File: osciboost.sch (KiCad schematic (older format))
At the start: 48 parts, among them P1 Molex 73137-5003, P2 BOOST_LEFT, P3 BOOST_RIGHT, P4 Molex 73137-5003, Q1 DMG1013T, U1 MA1702, U2 MAX6102, U3 LMV821AICT, U4 LMV821AICT, U5 LMV821AICT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

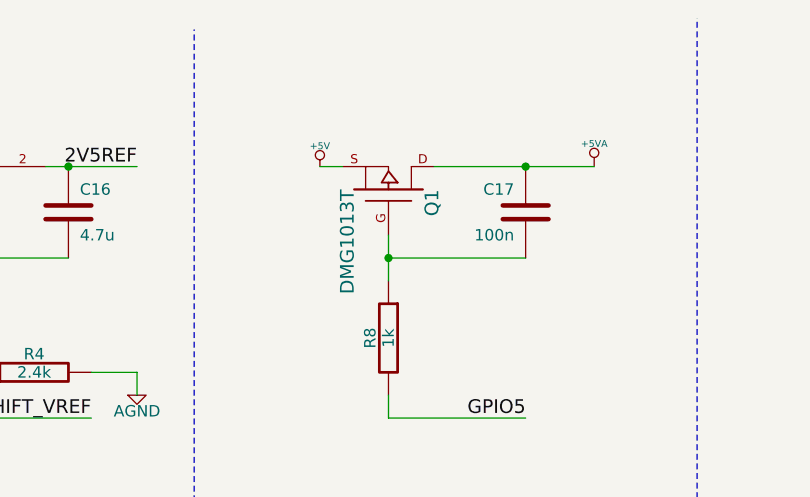
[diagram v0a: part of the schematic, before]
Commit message: Add pull-up resistor for the soft-start circuit
The microcontroller can never bring the voltage on the gate of the soft-start
MOSFET to the 5V needed to turn off power. To only way to achieve 5V is to have
a pull-up resistor, and let the control pin in high-impedance mode.
When the control pin is configured as an output, and (preferrably) set low, the
osciboost module will be powered on. To power off the module, the pin is put
into high-impedance mode.

Add a 10k pull-up resistor to enable the power-off circuit to function
correctly.

Signed-off-by: Alexandru Gagniuc <mr.nuke.me@gmail.com>
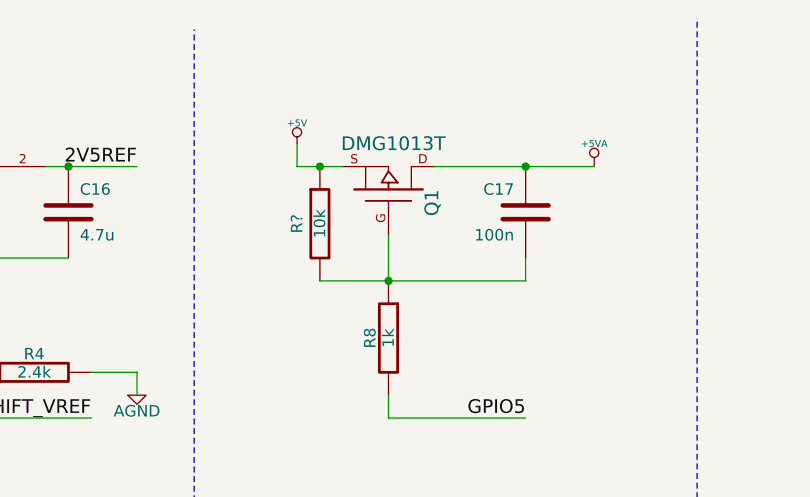
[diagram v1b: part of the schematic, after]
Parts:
- added R?: 10k, symbol R
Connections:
- net +5V: now also R?.1
- net at C17.2, Q1.G, R8.1: now also R?.2
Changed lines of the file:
@@
-EESchema Schematic File Version 2  date Mon 21 Jan 2013 01:50:25 PM CST
+EESchema Schematic File Version 2  date Mon 21 Jan 2013 09:27:00 PM CST
 LIBS:power
 LIBS:device
@@
 encoding utf-8
 Sheet 1 1
-Title "noname.sch"
-Date "21 jan 2013"
-Rev ""
-Comp ""
+Title "osciboost.sch"
+Date "22 jan 2013"
+Rev "NA"
+Comp "G-Tech Hardware Solutions"
 Comment1 ""
 Comment2 ""
@@
 Comment4 ""
 $EndDescr
+Connection ~ 5600 1600
+Wire Wire Line
+	5300 1600 6200 1600
+Wire Wire Line
+	6200 1600 6200 1500
+Connection ~ 5300 1100
 Wire Wire Line
 	9000 1400 8800 1400
@@
 	4750 2900 4750 500
 Wire Wire Line
-	6200 1500 5600 1500
-Connection ~ 5600 1500
-Wire Wire Line
 	6500 1100 5800 1100
 Connection ~ 6200 1100
-Wire Wire Line
-	5300 1100 5400 1100
 Wire Wire Line
 	6200 3750 6400 3750
@@
 Wire Wire Line
 	9000 1300 8800 1300
+Wire Wire Line
+	5200 1000 5200 1100
+Wire Wire Line
+	5200 1100 5400 1100
+$Comp
+L R R?
+U 1 1 50FE06D2
+P 5300 1350
+F 0 "R?" V 5200 1350 50  0000 C CNN
+F 1 "10k" V 5300 1350 50  0000 C CNN
+	1    5300 1350
+	1    0    0    -1
+$EndComp
 Text Label 9000 1400 2    60   ~ 0
 AIN2
@@
 L +5V #PWR024
 U 1 1 50FAE458
-P 5300 1100
-F 0 "#PWR024" H 5300 1190 20  0001 C CNN
-F 1 "+5V" H 5300 1190 30  0000 C CNN
-	1    5300 1100
+P 5200 1000
+F 0 "#PWR024" H 5200 1090 20  0001 C CNN
+F 1 "+5V" H 5200 1090 30  0000 C CNN
+	1    5200 1000
 	-1   0    0    -1
 $EndComp
@@
 P 5600 1200
 F 0 "Q1" H 5600 1390 60  0000 R CNN
-F 1 "DMG1013T" H 5600 1020 60  0000 R CNN
+F 1 "DMG1013T" V 5800 1450 60  0000 R CNN
 	1    5600 1200
 	0    1    -1   0

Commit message: Replace OPAMP with OPA1662 in MSOP-8 package
The previously selected opamps could only handle 6V, not the 10V we are feeding
them. Change the opamps to OPA1662, which have the desired characteristics.
Also, using dual opamps allows us to reduce the number of filter capacitors.

Because the change in footprint, re-laying part of the board was also needed.
The advantage is that the pinout of the MSOP-8 package is identical with many
other opamps.

Signed-off-by: Alexandru Gagniuc <mr.nuke.me@gmail.com>
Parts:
- removed C11, C15, C4, C6: 4.7u, symbol C
- U3: value LMV821AICT -> OPA1662; symbol LMV821AICT -> TL072
- U3: renamed from U4; value LMV821AICT -> OPA1662; symbol LMV821AICT -> TL072
- U4: renamed from U6; value LMV821AICT -> OPA1662; symbol LMV821AICT -> TL072
- U4: renamed from U5; value LMV821AICT -> OPA1662; symbol LMV821AICT -> TL072
- gave numbers to parts that had none: 1
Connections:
- net +5VA: now also U3.8 (V+), U3.8 (V+), U4.8 (V+), U4.8 (V+); no longer U3.5 (V+), U3.5 (V+), U4.5 (V+), U4.5 (V+)
- net -5VA: now also U3.4 (V-), U3.4 (V-), U4.4 (V-), U4.4 (V-); no longer U3.2 (V-), U3.2 (V-), U4.2 (V-), U4.2 (V-)
- net SHIFT_VREF: now also U3.3 (+), U4.3 (+); no longer U3.1 (+), U4.1 (+)
- net at C10.1, C9.2, R1.2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: now also U3.5 (+); no longer U3.1 (+)
- net at R5.2, R6.1: now also U3.6 (-); no longer U3.3 (-)
- net at R5.1, R7.1: now also U3.7; no longer U3.4
- net at R7.2, R9.2: now also U3.2 (-); no longer U3.3 (-)
- net at R10.1, R9.1: now also U3.1; no longer U3.4
- net at R16.1, R17.1: now also U4.1; no longer U4.4
- net at R13.2, R14.1: now also U4.6 (-); no longer U4.3 (-)
- net at R13.1, R15.1: now also U4.7; no longer U4.4
- net at R15.2, R16.2: now also U4.2 (-); no longer U4.3 (-)
- net at C19.2, C20.1, R11.2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: now also U4.5 (+); no longer U4.1 (+)
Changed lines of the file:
@@
-EESchema Schematic File Version 2  date Mon 21 Jan 2013 09:27:00 PM CST
+EESchema Schematic File Version 2  date Sat 26 Jan 2013 03:39:28 PM CST
 LIBS:power
 LIBS:device
@@
 Sheet 1 1
 Title "osciboost.sch"
-Date "22 jan 2013"
+Date "26 jan 2013"
 Rev "NA"
 Comp "G-Tech Hardware Solutions"
@@
 Comment4 ""
 $EndDescr
+Wire Wire Line
+	9300 3700 9000 3700
+Wire Wire Line
+	7300 3300 7600 3300
 Connection ~ 5600 1600
 Wire Wire Line
@@
 Connection ~ 9000 3700
 Connection ~ 9300 3700
-Wire Wire Line
-	9600 3700 8700 3700
 Connection ~ 9300 3300
 Wire Wire Line
-	8700 3300 9600 3300
-Connection ~ 7900 3700
-Wire Wire Line
-	7300 3700 8200 3700
-Connection ~ 7900 3300
-Wire Wire Line
-	7300 3300 8200 3300
-Wire Wire Line
 	9000 3200 9000 3300
 Wire Wire Line
-	7600 3200 7600 3300
+	7600 3300 7600 3200
 Wire Wire Line
 	7600 3800 7600 3700
@@
 Wire Wire Line
 	5200 1100 5400 1100
-$Comp
-L R R?
+Wire Wire Line
+	7600 3700 7300 3700
+Wire Wire Line
+	9000 3300 9300 3300
+$Comp
+L R R18
 U 1 1 50FE06D2
 P 5300 1350
-F 0 "R?" V 5200 1350 50  0000 C CNN
+F 0 "R18" V 5200 1350 50  0000 C CNN
 F 1 "10k" V 5300 1350 50  0000 C CNN
 	1    5300 1350
@@
 $EndComp
 $Comp
-L LMV821AICT U5
-U 1 1 50FD9AB6
+L TL072 U4
+U 2 1 50FD9AB6
 P 3100 6300
-F 0 "U5" H 3050 6500 60  0000 L CNN
-F 1 "LMV821AICT" H 3050 6050 60  0000 L CNN
-	1    3100 6300
-	1    0    0    -1
-$EndComp
-$Comp
-L LMV821AICT U6
+F 0 "U4" H 3050 6500 60  0000 L CNN
+F 1 "OPA1662" H 3050 6050 60  0000 L CNN
+	2    3100 6300
+	1    0    0    -1
+$EndComp
+$Comp
+L TL072 U4
 U 1 1 50FD9AB5
 P 5000 6200
-F 0 "U6" H 4950 6400 60  0000 L CNN
-F 1 "LMV821AICT" H 4950 5950 60  0000 L CNN
+F 0 "U4" H 4950 6400 60  0000 L CNN
+F 1 "OPA1662" H 4950 5950 60  0000 L CNN
 	1    5000 6200
 	1    0    0    -1
@@
 $EndComp
 $Comp
-L C C15
-U 1 1 50FB729E
-P 9600 3500
-F 0 "C15" H 9650 3600 50  0000 L CNN
-F 1 "4.7u" H 9650 3400 50  0000 L CNN
-	1    9600 3500
-	1    0    0    -1
-$EndComp
-$Comp
 L C C14
 U 1 1 50FB729B
@@
 $EndComp
 $Comp
-L C C6
-U 1 1 50FB7298
-P 8200 3500
-F 0 "C6" H 8250 3600 50  0000 L CNN
-F 1 "4.7u" H 8250 3400 50  0000 L CNN
-	1    8200 3500
-	1    0    0    -1
-$EndComp
-$Comp
-L C C4
-U 1 1 50FB7296
-P 7900 3500
-F 0 "C4" H 7950 3600 50  0000 L CNN
-F 1 "4.7u" H 7950 3400 50  0000 L CNN
-	1    7900 3500
-	1    0    0    -1
-$EndComp
-$Comp
 L C C12
 U 1 1 50FB7293
@@
 F 1 "4.7u" H 9050 3400 50  0000 L CNN
 	1    9000 3500
-	1    0    0    -1
-$EndComp
-$Comp
-L C C11
-U 1 1 50FB7290
-P 8700 3500
-F 0 "C11" H 8750 3600 50  0000 L CNN
-F 1 "4.7u" H 8750 3400 50  0000 L CNN
-	1    8700 3500
 	1    0    0    -1
 $EndComp
@@
 $EndComp
 $Comp
-L LMV821AICT U4
+L TL072 U3
 U 1 1 50F5C4AB
 P 5000 3750
-F 0 "U4" H 4950 3950 60  0000 L CNN
-F 1 "LMV821AICT" H 4950 3500 60  0000 L CNN
+F 0 "U3" H 4950 3950 60  0000 L CNN
+F 1 "OPA1662" H 4950 3500 60  0000 L CNN
 	1    5000 3750
 	1    0    0    -1
 $EndComp
 $Comp
-L LMV821AICT U3
-U 1 1 50F5C4A7
+L TL072 U3
+U 2 1 50F5C4A7
 P 3100 3850
 F 0 "U3" H 3050 4050 60  0000 L CNN
-F 1 "LMV821AICT" H 3050 3600 60  0000 L CNN
-	1    3100 3850
-	1    0    0    -1
-$EndComp
+F 1 "OPA1662" H 3050 3600 60  0000 L CNN
+	2    3100 3850
+	1    0    0    -1
+$EndComp

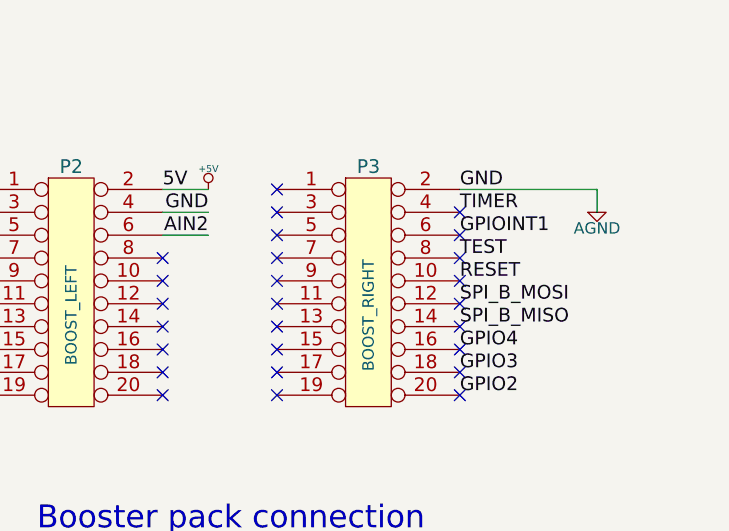
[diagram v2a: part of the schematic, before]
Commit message: Reorganize ground planes
Use only one ground analog plane; do not split it up in mini ground planes for
power, reference voltage etc. The previous layout routed the ground, AIN, and
power signals independently, creating a bunch of small antennas ready to pick up
noise. To solve this, join the analog ground plane near the AIN pins on the
connector, and route all signals (including power) above the join.

Decouple the ground planes from the ground pin on the right-side connector.
Ground currents could have leaked around the analog ground plane, through the
GND pin, creating a large antenna. Not having a ground path through the right
GND pin would break compatibility with 20-pin boards. To solve this issue, add
an optional 0 Ohm resistor that connects the analog ground plane to the ground
plane on the right side.

Signed-off-by: Alexandru Gagniuc <mr.nuke.me@gmail.com>
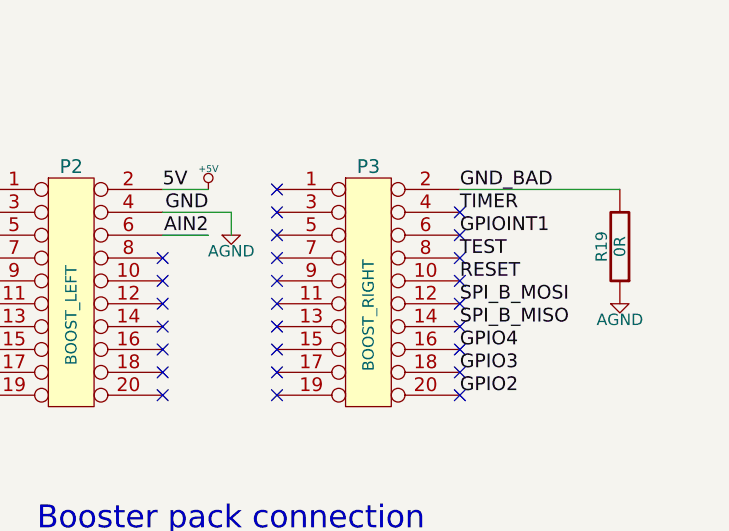
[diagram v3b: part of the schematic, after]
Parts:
- added R19: 0R, symbol R
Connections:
- net AGND: now also R19.1; no longer P3.2 (P2)
- new net GND_BAD: P3.2 (P2), R19.2
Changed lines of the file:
@@
-EESchema Schematic File Version 2  date Sat 26 Jan 2013 03:39:28 PM CST
+EESchema Schematic File Version 2  date Sat 26 Jan 2013 06:13:08 PM CST
 LIBS:power
 LIBS:device
@@
 Sheet 1 1
 Title "osciboost.sch"
-Date "26 jan 2013"
+Date "27 jan 2013"
 Rev "NA"
 Comp "G-Tech Hardware Solutions"
@@
 $EndDescr
 Wire Wire Line
+	9100 1300 9100 1400
+Wire Wire Line
+	8800 1300 9100 1300
+Wire Wire Line
 	9300 3700 9000 3700
 Wire Wire Line
@@
 Wire Wire Line
 	9000 1400 8800 1400
-Wire Wire Line
-	10700 1300 10700 1200
-Wire Wire Line
-	10700 1200 10100 1200
 Wire Notes Line
 	6950 5400 450  5400
@@
 	6950 7800 6950 450
 Wire Wire Line
-	9000 1300 8800 1300
-Wire Wire Line
 	5200 1000 5200 1100
 Wire Wire Line
@@
 Wire Wire Line
 	9000 3300 9300 3300
+Wire Wire Line
+	10800 1200 10100 1200
+$Comp
+L AGND #PWR?
+U 1 1 5104710D
+P 9100 1400
+F 0 "#PWR?" H 9100 1400 40  0001 C CNN
+F 1 "AGND" H 9100 1330 50  0000 C CNN
+	1    9100 1400
+	1    0    0    -1
+$EndComp
+$Comp
+L R R19
+U 1 1 51046F2E
+P 10800 1450
+F 0 "R19" V 10880 1450 50  0000 C CNN
+F 1 "0R" V 10800 1450 50  0000 C CNN
+	1    10800 1450
+	-1   0    0    1
+$EndComp
 $Comp
 L R R18
@@
 L AGND #PWR025
 U 1 1 50FAE430
-P 10700 1300
-F 0 "#PWR025" H 10700 1300 40  0001 C CNN
-F 1 "AGND" H 10700 1230 50  0000 C CNN
-	1    10700 1300
+P 10800 1700
+F 0 "#PWR025" H 10800 1700 40  0001 C CNN
+F 1 "AGND" H 10800 1630 50  0000 C CNN
+	1    10800 1700
 	1    0    0    -1
 $EndComp
@@
 TIMER
 Text Label 10100 1200 0    60   ~ 0
-GND
+GND_BAD
 Text Label 10100 1500 0    60   ~ 0
 TEST
